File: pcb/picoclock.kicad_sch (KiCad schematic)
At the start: 54 parts, among them J1 UART, J10 USB, J2 AUDIO, J3 xx, J4 xx, J5 Power In, J6 USB_C_Receptacle, J7 xx, J8 xx, J9 screen_adapter_connector, SW1 SW_Push, SW2 SW_Push, SW3 SW_Push, SW4 SW_Push, SW5 SW_Push, SW6 SW_Push, U1 PCF8563T, U2 Pico, U3 MCP9808_MSOP, U4 PCM5100, Y1 Crystal

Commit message: update case+pcb
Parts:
- added R10, R11, R12, R13, R8, R9: 10K, Resistor_SMD:R_0603_1608Metric, symbol Device:R
- H1, H2, H3, H4: footprint MountingHole:MountingHole_2.5mm -> MountingHole:MountingHole_3mm_Pad; symbol Mechanical:MountingHole -> Mechanical:MountingHole_Pad
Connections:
- net +3.3V: now also R10.1, R11.1, R12.1, R13.1, R8.1, R9.1
- net GND: now also H1.1, H2.1, H3.1, H4.1
- net GPIO10: now also R12.2
- net GPIO19: now also R11.2
- net GPIO20: now also R10.2
- net GPIO21: now also R9.2
- net GPIO8: now also R8.2
- net GPIO9: now also R13.2
- net SCL: now also J4.5 (Pin_5)
- net SDA: now also J4.4 (Pin_4)
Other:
- moved on the sheet: SW4, SW5, SW6

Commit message: [pcb] update
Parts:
- added BT1: 3V Cell, cell:MPD_BC501SM-TR, symbol Device:Battery_Cell
- added J11: Alt Power, Connector_PinHeader_2.54mm:PinHeader_1x02_P2.54mm_Vertical, symbol Connector:Conn_01x02_Pin
- C1, C2, C3, C4, C5, C9: footprint Capacitor_SMD:C_0402_1005Metric -> Capacitor_SMD:C_0603_1608Metric
- R2, R4: footprint Resistor_SMD:R_0402_1005Metric -> Resistor_SMD:R_0603_1608Metric
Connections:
- net +3.3V: now also J11.2 (Pin_2); no longer C2.1, U1.8 (VDD)
- net GND: now also BT1.2 (-)
- new net 3V BATT: BT1.1 (+), C2.1, J11.1 (Pin_1), U1.8 (VDD)
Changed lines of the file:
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@@
   (junction (at 243.84 40.64) (diameter 0) (color 0 0 0 0)
   )
+  (junction (at 46.99 161.29) (diameter 0) (color 0 0 0 0)
+  )
   (junction (at 45.085 132.715) (diameter 0) (color 0 0 0 0)
   )
@@
   (junction (at 107.95 160.02) (diameter 0) (color 0 0 0 0)
   )
-  (junction (at 50.8 161.29) (diameter 0) (color 0 0 0 0)
-  )
   (junction (at 37.465 171.45) (diameter 0) (color 0 0 0 0)
   )
@@
     (stroke (width 0) (type default))
   )
+  (wire (pts (xy 46.99 161.29) (xy 50.8 161.29))
+    (stroke (width 0) (type default))
+  )
   (wire (pts (xy 90.17 47.625) (xy 90.17 50.165))
     (stroke (width 0) (type default))
   )
-  (wire (pts (xy 40.005 161.29) (xy 50.8 161.29))
+  (wire (pts (xy 32.385 161.29) (xy 46.99 161.29))
     (stroke (width 0) (type default))
   )
@@
     (stroke (width 0) (type default))
   )
+  (wire (pts (xy 46.99 156.845) (xy 46.99 161.29))
+    (stroke (width 0) (type default))
+  )
   (wire (pts (xy 86.36 50.165) (xy 87.63 50.165))
     (stroke (width 0) (type default))
@@
     (stroke (width 0) (type default))
   )
+  (wire (pts (xy 46.99 156.845) (xy 48.895 156.845))
+    (stroke (width 0) (type default))
+  )
   (wire (pts (xy 100.33 70.485) (xy 100.33 72.39))
     (stroke (width 0) (type default))
@@
     (stroke (width 0) (type default))
   )
-  (wire (pts (xy 40.005 161.29) (xy 40.005 158.75))
-    (stroke (width 0) (type default))
-  )
   (wire (pts (xy 95.885 72.39) (xy 97.79 72.39))
     (stroke (width 0) (type default))
@@
     )
   )
+  (global_label "3V BATT" (shape input) (at 34.925 161.29 90) (fields_autoplaced)
+    (effects (font (size 1.27 1.27)) (justify left))
+    (property "Intersheetrefs" "${INTERSHEET_REFS}" (at 34.925 150.7453 90)
+      (effects (font (size 1.27 1.27)) (justify left) hide)
+    )
+  )
   (global_label "GPIO2 SCREEN DATA" (shape input) (at 240.665 118.11 270) (fields_autoplaced)
     (effects (font (size 1.27 1.27)) (justify right))
@@
     (effects (font (size 1.27 1.27)) (justify right))
   )
+  (symbol (lib_id "Device:Battery_Cell") (at 27.305 161.29 270) (unit 1)
+    (in_bom yes) (on_board yes) (dnp no) (fields_autoplaced)
+    (property "Reference" "BT1" (at 29.1465 154.6225 90)
+      (effects (font (size 1.27 1.27)))
+    )
+    (property "Value" "3V Cell" (at 29.1465 157.1625 90)
+      (effects (font (size 1.27 1.27)))
+    )
+    (property "Footprint" "cell:MPD_BC501SM-TR" (at 28.829 161.29 90)
+      (effects (font (size 1.27 1.27)) hide)
+    )
+    (property "Datasheet" "~" (at 28.829 161.29 90)
+      (effects (font (size 1.27 1.27)) hide)
+    )
+    (pin "2")
+    (pin "1")
+    (instances
+      (project "picoclock"
+        (path "/3b9dec0e-e0b7-4565-afc9-c4692f41aea9"
+          (reference "BT1") (unit 1)
+        )
+      )
+    )
+  )
   (symbol (lib_id "Device:R") (at 136.525 100.33 0) (unit 1)
     (in_bom yes) (on_board yes) (dnp no)
@@
     )
   )
+  (symbol (lib_id "power:+3.3V") (at 48.895 154.305 90) (unit 1)
+    (in_bom yes) (on_board yes) (dnp no)
+    (property "Reference" "#PWR03" (at 52.705 154.305 0)
+      (effects (font (size 1.27 1.27)) hide)
+    )
+    (property "Value" "+3.3V" (at 45.085 153.67 0)
+      (effects (font (size 1.27 1.27)))
+    )
+    (property "Footprint" "" (at 48.895 154.305 0)
+      (effects (font (size 1.27 1.27)) hide)
+    )
+    (property "Datasheet" "" (at 48.895 154.305 0)
+      (effects (font (size 1.27 1.27)) hide)
+    )
+    (pin "1")
+    (instances
+      (project "picoclock"
+        (path "/3b9dec0e-e0b7-4565-afc9-c4692f41aea9"
+          (reference "#PWR03") (unit 1)
+        )
+      )
+    )
+  )
   (symbol (lib_id "power:+3.3V") (at 136.525 120.015 270) (unit 1)
     (in_bom yes) (on_board yes) (dnp no)
@@
       (effects (font (size 1.27 1.27)))
     )
-    (property "Footprint" "Capacitor_SMD:C_0402_1005Metric" (at 99.06 157.48 0)
+    (property "Footprint" "Capacitor_SMD:C_0603_1608Metric" (at 99.06 157.48 0)
       (effects (font (size 1.27 1.27)) hide)
     )
@@
       (effects (font (size 1.27 1.27)))
     )
-    (property "Footprint" "Capacitor_SMD:C_0402_1005Metric" (at 156.21 175.895 0)
+    (property "Footprint" "Capacitor_SMD:C_0603_1608Metric" (at 156.21 175.895 0)
       (effects (font (size 1.27 1.27)) hide)
     )
@@
       (effects (font (size 1.27 1.27)))
     )
-    (property "Footprint" "Resistor_SMD:R_0402_1005Metric" (at 156.21 158.115 0)
+    (property "Footprint" "Resistor_SMD:R_0603_1608Metric" (at 156.21 158.115 0)
       (effects (font (size 1.27 1.27)) hide)
     )
@@
     )
   )
+  (symbol (lib_id "power:GND") (at 24.765 161.29 270) (unit 1)
+    (in_bom yes) (on_board yes) (dnp no) (fields_autoplaced)
+    (property "Reference" "#PWR069" (at 18.415 161.29 0)
+      (effects (font (size 1.27 1.27)) hide)
+    )
+    (property "Value" "GND" (at 20.955 161.29 90)
+      (effects (font (size 1.27 1.27)) (justify right))
+    )
+    (property "Footprint" "" (at 24.765 161.29 0)
+      (effects (font (size 1.27 1.27)) hide)
+    )
+    (property "Datasheet" "" (at 24.765 161.29 0)
+      (effects (font (size 1.27 1.27)) hide)
+    )
+    (pin "1")
+    (instances
+      (project "picoclock"
+        (path "/3b9dec0e-e0b7-4565-afc9-c4692f41aea9"
+          (reference "#PWR069") (unit 1)
+        )
+      )
+    )
+  )
   (symbol (lib_id "Device:C_Small") (at 153.67 167.005 0) (unit 1)
     (in_bom yes) (on_board yes) (dnp no) (fields_autoplaced)
@@
       (effects (font (size 1.27 1.27)))
     )
-    (property "Footprint" "Capacitor_SMD:C_0402_1005Metric" (at 103.505 157.48 0)
+    (property "Footprint" "Capacitor_SMD:C_0603_1608Metric" (at 103.505 157.48 0)
       (effects (font (size 1.27 1.27)) hide)
     )
@@
     )
   )
-  (symbol (lib_id "power:+3.3V") (at 40.005 158.75 0) (unit 1)
-    (in_bom yes) (on_board yes) (dnp no) (fields_autoplaced)
-    (property "Reference" "#PWR03" (at 40.005 162.56 0)
-      (effects (font (size 1.27 1.27)) hide)
-    )
-    (property "Value" "+3.3V" (at 40.005 153.67 0)
-      (effects (font (size 1.27 1.27)))
-    )
-    (property "Footprint" "" (at 40.005 158.75 0)
-      (effects (font (size 1.27 1.27)) hide)
-    )
-    (property "Datasheet" "" (at 40.005 158.75 0)
-      (effects (font (size 1.27 1.27)) hide)
-    )
-    (pin "1")
-    (instances
-      (project "picoclock"
-        (path "/3b9dec0e-e0b7-4565-afc9-c4692f41aea9"
-          (reference "#PWR03") (unit 1)
-        )
-      )
-    )
-  )
   (symbol (lib_id "power:+5V") (at 105.41 56.515 180) (unit 1)
     (in_bom yes) (on_board yes) (dnp no)
@@
       (effects (font (size 1.27 1.27)))
     )
-    (property "Footprint" "Capacitor_SMD:C_0402_1005Metric" (at 30.48 171.45 0)
+    (property "Footprint" "Capacitor_SMD:C_0603_1608Metric" (at 30.48 171.45 0)
       (effects (font (size 1.27 1.27)) hide)
     )
@@
       (effects (font (size 1.27 1.27)))
     )
-    (property "Footprint" "Capacitor_SMD:C_0402_1005Metric" (at 75.565 161.29 0)
+    (property "Footprint" "Capacitor_SMD:C_0603_1608Metric" (at 75.565 161.29 0)
       (effects (font (size 1.27 1.27)) hide)
     )
@@
     )
   )
+  (symbol (lib_id "Connector:Conn_01x02_Pin") (at 53.975 156.845 180) (unit 1)
+    (in_bom yes) (on_board yes) (dnp no)
+    (property "Reference" "J11" (at 51.435 158.75 0)
+      (effects (font (size 1.27 1.27)))
+    )
+    (property "Value" "Alt Power" (at 55.88 154.94 90)
+      (effects (font (size 1.27 1.27)))
+    )
+    (property "Footprint" "Connector_PinHeader_2.54mm:PinHeader_1x02_P2.54mm_Vertical" (at 53.975 156.845 0)
+      (effects (font (size 1.27 1.27)) hide)
+    )
+    (property "Datasheet" "~" (at 53.975 156.845 0)
+      (effects (font (size 1.27 1.27)) hide)
+    )
+    (pin "1")
+    (pin "2")
+    (instances
+      (project "picoclock"
+        (path "/3b9dec0e-e0b7-4565-afc9-c4692f41aea9"
+          (reference "J11") (unit 1)
+        )
+      )
+    )
+  )
   (symbol (lib_id "Connector:Conn_01x08_Socket") (at 168.91 28.575 270) (mirror x) (unit 1)
     (in_bom yes) (on_board yes) (dnp no)
@@
       (effects (font (size 1.27 1.27)))
     )
-    (property "Footprint" "Resistor_SMD:R_0402_1005Metric" (at 156.21 155.575 0)
+    (property "Footprint" "Resistor_SMD:R_0603_1608Metric" (at 156.21 155.575 0)
       (effects (font (size 1.27 1.27)) hide)
     )
@@
       (effects (font (size 1.27 1.27)))
     )
-    (property "Footprint" "Capacitor_SMD:C_0402_1005Metric" (at 107.95 157.48 0)
+    (property "Footprint" "Capacitor_SMD:C_0603_1608Metric" (at 107.95 157.48 0)
       (effects (font (size 1.27 1.27)) hide)
     )

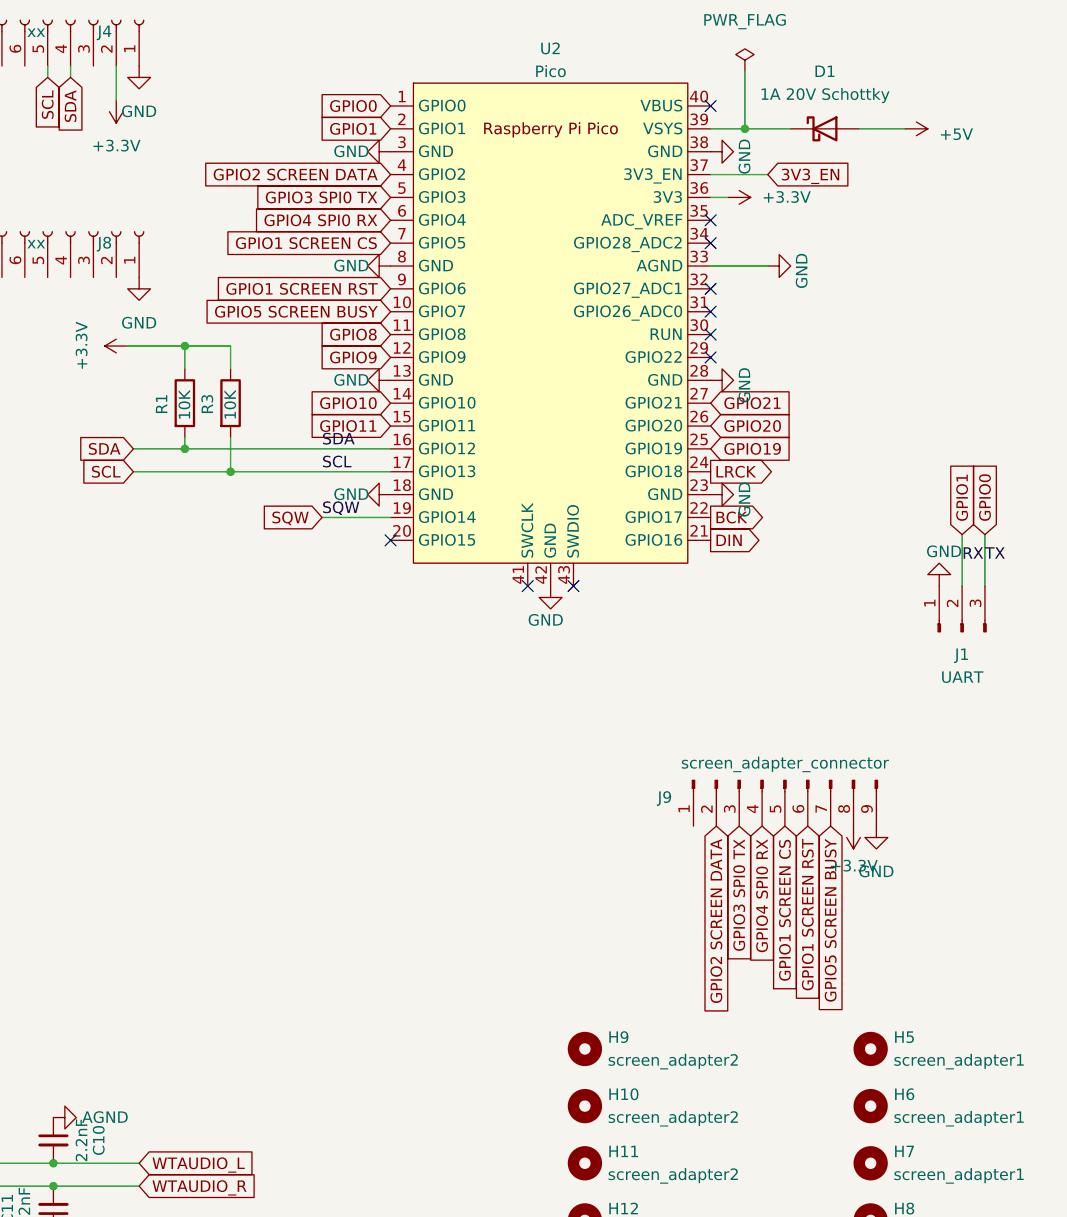
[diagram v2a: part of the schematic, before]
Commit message: [pcb] fix epaper hat position, fix GPIO, add labels
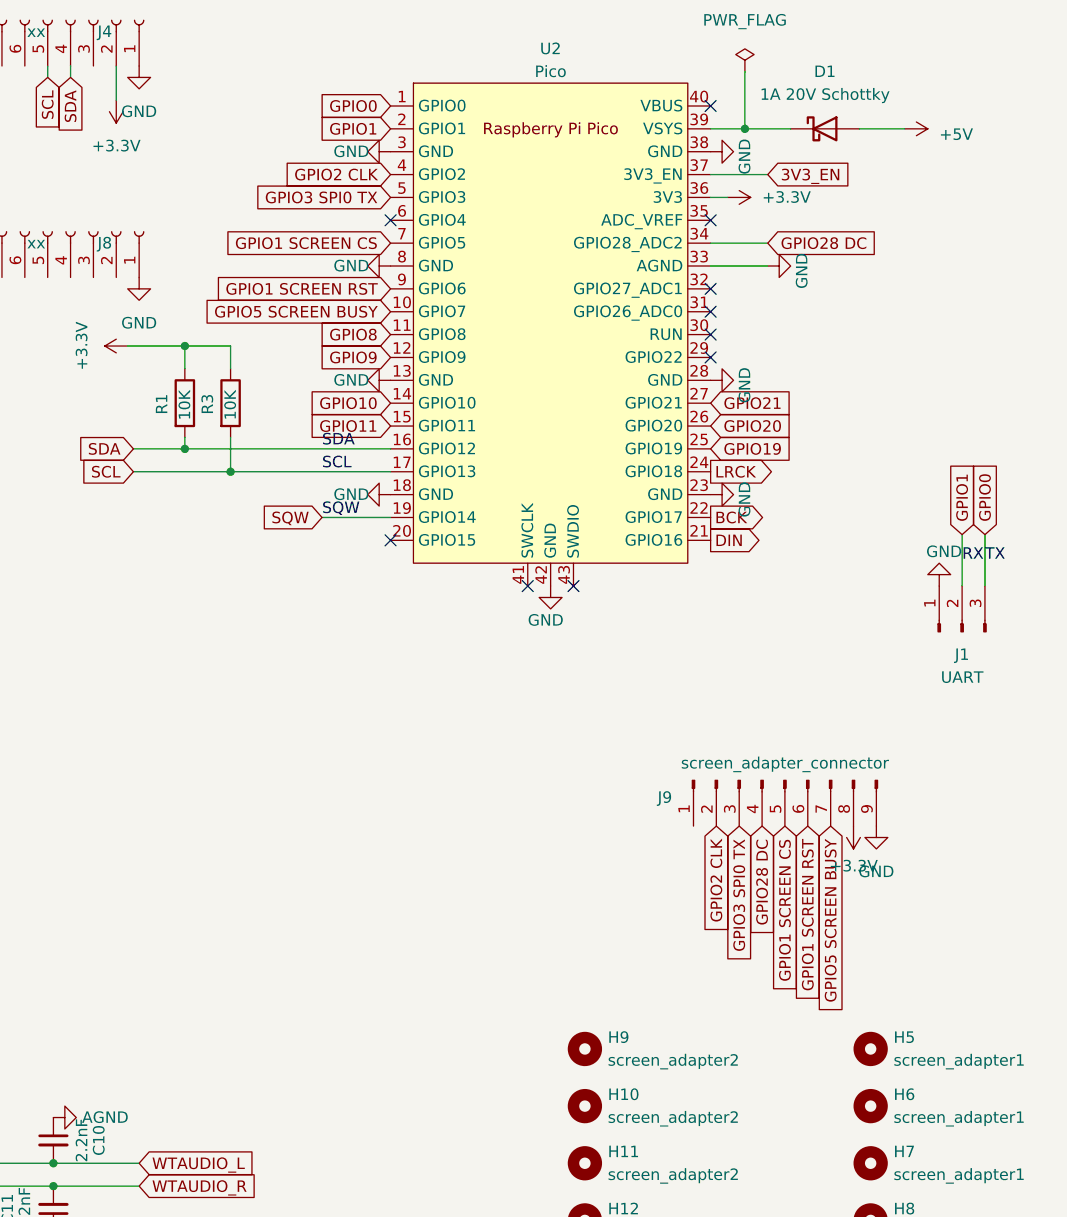
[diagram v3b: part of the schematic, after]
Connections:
- net GPIO28 DC: now reaches U2.34 (GPIO28_ADC2)
- net GPIO28 DC: now also J9.4 (Pin_4)
- net GPIO2 SCREEN DATA renamed GPIO2 CLK
- net GPIO4 SPI0 RX: no longer names the net of U2.6 (GPIO4)
- net GPIO4 SPI0 RX: no longer J9.4 (Pin_4)
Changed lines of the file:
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@@
   (no_connect (at 224.79 91.44))
   (no_connect (at 240.03 50.8))
-  (no_connect (at 240.03 53.34))
   (no_connect (at 240.03 63.5))
   (no_connect (at 240.03 38.1))
   (no_connect (at 204.47 86.36))
   (no_connect (at 240.03 60.96))
+  (no_connect (at 204.47 50.8))
   (wire (pts (xy 127 168.275) (xy 127 170.815))
     (stroke (width 0) (type default))
@@
     (stroke (width 0) (type default))
   )
+  (wire (pts (xy 246.38 53.34) (xy 240.03 53.34))
+    (stroke (width 0) (type default))
+  )
   (wire (pts (xy 138.43 104.14) (xy 136.525 104.14))
     (stroke (width 0) (type default))
@@
     )
   )
+  (global_label "GPIO2 CLK" (shape input) (at 240.665 118.11 270) (fields_autoplaced)
+    (effects (font (size 1.27 1.27)) (justify right))
+    (property "Intersheetrefs" "${INTERSHEET_REFS}" (at 240.665 131.3157 90)
+      (effects (font (size 1.27 1.27)) (justify right) hide)
+    )
+  )
   (global_label "1~{PRE}" (shape input) (at 63.5 181.61 0) (fields_autoplaced)
     (effects (font (size 1.27 1.27)) (justify left))
@@
     )
   )
-  (global_label "GPIO4 SPI0 RX" (shape input) (at 204.47 50.8 180) (fields_autoplaced)
-    (effects (font (size 1.27 1.27)) (justify right))
-    (property "Intersheetrefs" "${INTERSHEET_REFS}" (at 187.0915 50.8 0)
-      (effects (font (size 1.27 1.27)) (justify right) hide)
-    )
-  )
   (global_label "GPIO21" (shape input) (at 240.03 71.12 0) (fields_autoplaced)
     (effects (font (size 1.27 1.27)) (justify left))
@@
     )
   )
-  (global_label "GPIO2 SCREEN DATA" (shape input) (at 240.665 118.11 270) (fields_autoplaced)
-    (effects (font (size 1.27 1.27)) (justify right))
-    (property "Intersheetrefs" "${INTERSHEET_REFS}" (at 240.665 140.508 90)
-      (effects (font (size 1.27 1.27)) (justify right) hide)
-    )
-  )
   (global_label "USB D+" (shape input) (at 65.405 73.025 90) (fields_autoplaced)
     (effects (font (size 1.27 1.27)) (justify left))
@@
     )
   )
+  (global_label "GPIO28 DC" (shape input) (at 245.745 118.11 270) (fields_autoplaced)
+    (effects (font (size 1.27 1.27)) (justify right))
+    (property "Intersheetrefs" "${INTERSHEET_REFS}" (at 245.745 131.4971 90)
+      (effects (font (size 1.27 1.27)) (justify right) hide)
+    )
+  )
   (global_label "3V3_EN" (shape input) (at 246.38 45.72 0) (fields_autoplaced)
     (effects (font (size 1.27 1.27)) (justify left))
@@
     )
   )
-  (global_label "GPIO4 SPI0 RX" (shape input) (at 245.745 118.11 270) (fields_autoplaced)
-    (effects (font (size 1.27 1.27)) (justify right))
-    (property "Intersheetrefs" "${INTERSHEET_REFS}" (at 245.745 135.4885 90)
-      (effects (font (size 1.27 1.27)) (justify right) hide)
+  (global_label "GPIO28 DC" (shape input) (at 246.38 53.34 0) (fields_autoplaced)
+    (effects (font (size 1.27 1.27)) (justify left))
+    (property "Intersheetrefs" "${INTERSHEET_REFS}" (at 259.7671 53.34 0)
+      (effects (font (size 1.27 1.27)) (justify left) hide)
     )
   )
@@
     )
   )
-  (global_label "GPIO2 SCREEN DATA" (shape input) (at 204.47 45.72 180) (fields_autoplaced)
-    (effects (font (size 1.27 1.27)) (justify right))
-    (property "Intersheetrefs" "${INTERSHEET_REFS}" (at 182.072 45.72 0)
-      (effects (font (size 1.27 1.27)) (justify right) hide)
-    )
+  (global_label "GPIO2 CLK" (shape input) (at 204.47 45.72 180) (fields_autoplaced)
+    (effects (font (size 1.27 1.27)) (justify right))
+    (property "Intersheetrefs" "${INTERSHEET_REFS}" (at 191.2643 45.72 0)
+      (effects (font (size 1.27 1.27)) (justify right) hide)
+    )
